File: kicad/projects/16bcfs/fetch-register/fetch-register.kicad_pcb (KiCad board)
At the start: 4 copper layers, 101.8 x 61 mm, 116 parts, among them J1 InstrReg, J10 Address Bus 2, J11 ALU Bus B, J12 Main Bus, J13 Control Signals, J14 Power, J15 Power, J2 MemBus1, J3 Address Bus 2, J4 ALU Bus B, J5 Main Bus, J6 Control Signals, J7 Power, J8 InstrReg, J9 MemBus1, U1 74HC541, U10 74HC541, U11 74HC574, U12 74HC574, U13 74HC541, U2 74HC541, U3 74HC541, U4 74HC541, U5 74HC541, U6 74HC541, U7 74HC541, U8 74HC541, U9 74HC541

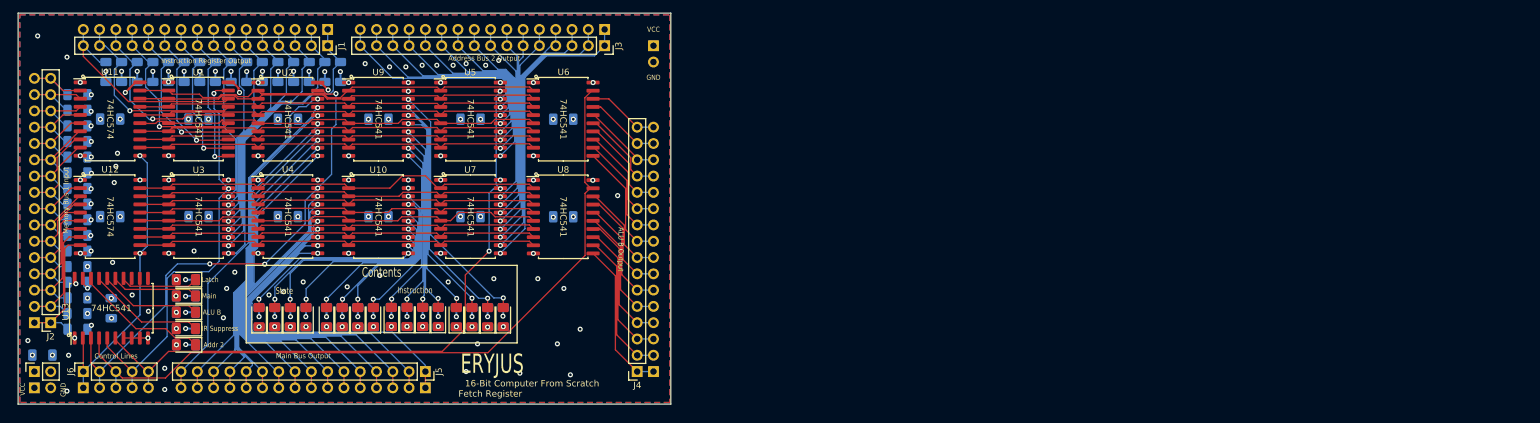
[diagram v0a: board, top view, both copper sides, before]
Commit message: Update the big-picture component placement
For the Fetch Register, all components needed to be removed and
re-placed into the PCB.  This commit is a first cut at that placement to
try to arrange the PCB.  The PCB can be shrunk quite a bit (maybe by
25%?) and this commit preceeds those changes.

Some changes were made to the schematic in order to drive more
efficient trace routing.
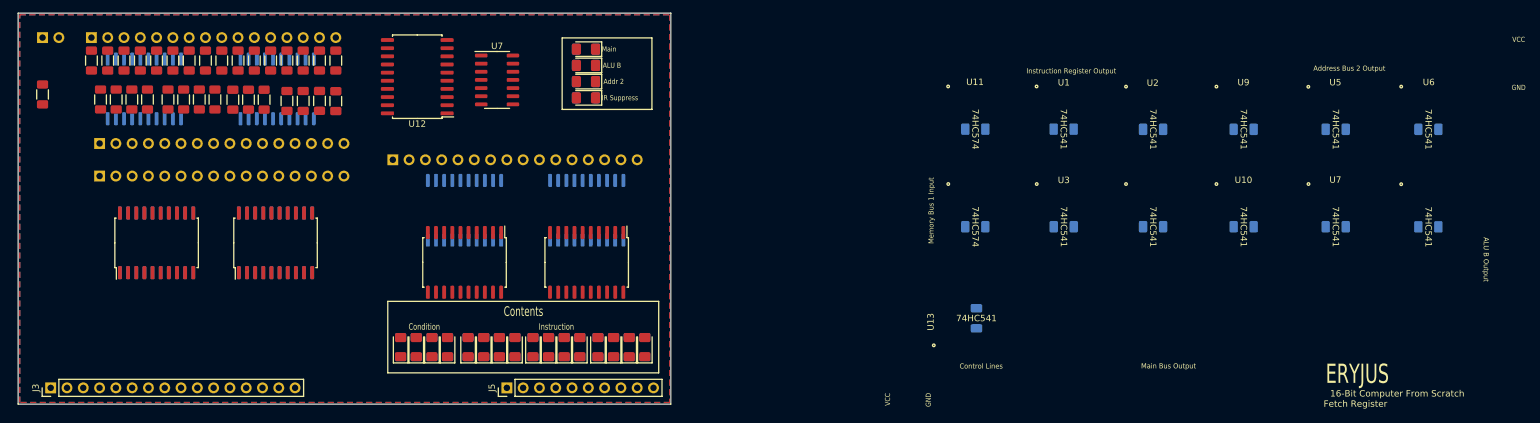
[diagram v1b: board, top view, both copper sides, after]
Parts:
- removed C14: 47uF, Capacitor_SMD:C_1206_3216Metric_Pad1.33x1.80mm_HandSolder
- removed D21: Red, LED_SMD:LED_1206_3216Metric_Pad1.42x1.75mm_HandSolder
- removed J10: Address Bus 2, Connector_PinHeader_2.54mm:PinHeader_1x16_P2.54mm_Vertical
- removed J11: ALU Bus B, Connector_PinHeader_2.54mm:PinHeader_1x16_P2.54mm_Vertical
- removed J12: Main Bus, Connector_PinHeader_2.54mm:PinHeader_1x16_P2.54mm_Vertical
- removed J13: Control Signals, Connector_PinHeader_2.54mm:PinHeader_1x05_P2.54mm_Vertical
- removed J14, J15: Power, Connector_PinHeader_2.54mm:PinHeader_1x02_P2.54mm_Vertical
- removed J8: InstrReg, Connector_PinHeader_2.54mm:PinHeader_1x16_P2.54mm_Vertical
- removed J9: MemBus1, Connector_PinHeader_2.54mm:PinHeader_1x16_P2.54mm_Vertical
- removed R53: 1K, Resistor_SMD:R_1206_3216Metric_Pad1.30x1.75mm_HandSolder
- removed U13: 74HC541, Package_SO:SOIC-20W_7.5x12.8mm_P1.27mm
- C12, C13: value 0.1uF -> 47uF
- J1: value InstrReg -> InstrRegInput; footprint Connector_PinSocket_2.54mm:PinSocket_1x16_P2.54mm_Vertical -> Connector_PinHeader_2.54mm:PinHeader_1x16_P2.54mm_Vertical; moved to B.Cu
- J2: value MemBus1 -> ALU Bus B; footprint Connector_PinSocket_2.54mm:PinSocket_1x16_P2.54mm_Vertical -> Connector_PinHeader_2.54mm:PinHeader_1x16_P2.54mm_Vertical; moved to B.Cu
- J3: value Address Bus 2 -> FetchBusInput; footprint Connector_PinSocket_2.54mm:PinSocket_1x16_P2.54mm_Vertical -> Connector_PinHeader_2.54mm:PinHeader_1x16_P2.54mm_Vertical
- J4: value ALU Bus B -> Main Bus; footprint Connector_PinSocket_2.54mm:PinSocket_1x16_P2.54mm_Vertical -> Connector_PinHeader_2.54mm:PinHeader_1x16_P2.54mm_Vertical; moved to B.Cu
- J5: value Main Bus -> Control Signals; footprint Connector_PinSocket_2.54mm:PinSocket_1x16_P2.54mm_Vertical -> Connector_PinHeader_2.54mm:PinHeader_1x10_P2.54mm_Vertical
- J6: value Control Signals -> Address Bus 2; footprint Connector_PinSocket_2.54mm:PinSocket_1x05_P2.54mm_Vertical -> Connector_PinHeader_2.54mm:PinHeader_1x16_P2.54mm_Vertical; moved to B.Cu
- J7: footprint Connector_PinSocket_2.54mm:PinSocket_1x02_P2.54mm_Vertical -> Connector_PinHeader_2.54mm:PinHeader_1x02_P2.54mm_Vertical; moved to B.Cu
- R21, R22, R23, R24, R25, R26, R27, R28, R29, R30, R31, R32, R33, R34, R35, R36, R37, R38, R39, R40, R41, R42, R43, R44, R45, R46, R47, R48, R49, R50, R51, R52: value 1K -> 10K; moved to F.Cu
- U1, U2, U5, U6: value 74HC541 -> 74HC574
- U10, U3, U4, U8, U9: value 74HC541 -> 74HC574; moved to B.Cu
- U11: moved to B.Cu
- U12: value 74HC574 -> 74HC541
- U7: value 74HC541 -> 74HC04; footprint Package_SO:SOIC-20W_7.5x12.8mm_P1.27mm -> Package_SO:SOIC-14_3.9x8.7mm_P1.27mm
- moved C10 134.9 mm to (213.9, 48.5)
- moved C2 134.9 mm to (199.8, 33.4)
- moved C4 134.9 mm to (199.8, 48.5)
- moved C5 134.9 mm to (228.3, 33.4)
- moved C7 134.9 mm to (228.3, 48.5)
- moved C9 134.9 mm to (213.9, 33.4)
- moved C1 134.9 mm to (185.9, 33.3)
- moved C13 134.9 mm to (172.3, 62.8)
- moved C3 134.9 mm to (185.9, 48.5)
- moved C6 134.9 mm to (242.7, 33.4)
- moved C8 134.9 mm to (242.7, 48.6)
- moved C11 134.9 mm to (172.1, 33.3)
- moved C12 134.9 mm to (172.1, 48.5)
- moved J3 101.5 mm to (27.9, 73.7), turned to 90 degrees
- moved R1 94.3 mm to (120.6, 67.3)
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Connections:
- D17 pad 1: /Latch LED -> /Main LED
- D18 pad 1: /Main LED -> /ALU B LED
- D19 pad 1: /ALU B LED -> /InstrReg LED
- D20 pad 1: /InstrReg LED -> /AddrBus2 LED
- J2 pad 1: MemBus1Bit0 -> ALUBBit0
- J2 pad 10: MemBus1Bit9 -> ALUBBit9
- J2 pad 11: MemBus1BitA -> ALUBBitA
- J2 pad 12: MemBus1BitB -> ALUBBitB
- J2 pad 13: MemBus1BitC -> ALUBBitC
- J2 pad 14: MemBus1BitD -> ALUBBitD
- J2 pad 15: MemBus1BitE -> ALUBBitE
- J2 pad 16: MemBus1BitF -> ALUBBitF
- J2 pad 2: MemBus1Bit1 -> ALUBBit1
- J2 pad 3: MemBus1Bit2 -> ALUBBit2
- J2 pad 4: MemBus1Bit3 -> ALUBBit3
- J2 pad 5: MemBus1Bit4 -> ALUBBit4
- J2 pad 6: MemBus1Bit5 -> ALUBBit5
- J2 pad 7: MemBus1Bit6 -> ALUBBit6
- J2 pad 8: MemBus1Bit7 -> ALUBBit7
- J2 pad 9: MemBus1Bit8 -> ALUBBit8
- J3 pad 1: AddrBus2Bit0 -> FetchBusBit0
- J3 pad 10: AddrBus2Bit9 -> FetchBusBit9
- J3 pad 11: AddrBus2BitA -> FetchBusBitA
- J3 pad 12: AddrBus2BitB -> FetchBusBitB
- J3 pad 13: AddrBus2BitC -> FetchBusBitC
- J3 pad 14: AddrBus2BitD -> FetchBusBitD
- J3 pad 15: AddrBus2BitE -> FetchBusBitE
- J3 pad 16: AddrBus2BitF -> FetchBusBitF
- J3 pad 2: AddrBus2Bit1 -> FetchBusBit1
- J3 pad 3: AddrBus2Bit2 -> FetchBusBit2
- J3 pad 4: AddrBus2Bit3 -> FetchBusBit3
- J3 pad 5: AddrBus2Bit4 -> FetchBusBit4
- J3 pad 6: AddrBus2Bit5 -> FetchBusBit5
- J3 pad 7: AddrBus2Bit6 -> FetchBusBit6
- J3 pad 8: AddrBus2Bit7 -> FetchBusBit7
- J3 pad 9: AddrBus2Bit8 -> FetchBusBit8
- J4 pad 1: ALUBBit0 -> MainBit0
- J4 pad 10: ALUBBit9 -> MainBit9
- J4 pad 11: ALUBBitA -> MainBitA
- J4 pad 12: ALUBBitB -> MainBitB
- J4 pad 13: ALUBBitC -> MainBitC
- J4 pad 14: ALUBBitD -> MainBitD
- J4 pad 15: ALUBBitE -> MainBitE
- J4 pad 16: ALUBBitF -> MainBitF
- J4 pad 2: ALUBBit1 -> MainBit1
- J4 pad 3: ALUBBit2 -> MainBit2
- J4 pad 4: ALUBBit3 -> MainBit3
- J4 pad 5: ALUBBit4 -> MainBit4
- J4 pad 6: ALUBBit5 -> MainBit5
- J4 pad 7: ALUBBit6 -> MainBit6
- J4 pad 8: ALUBBit7 -> MainBit7
- J4 pad 9: ALUBBit8 -> MainBit8
- J5 pad 1: MainBit0 -> CpuClk
- J5 pad 10: MainBit9 -> GNDREF
- J5 pad 2: MainBit1 -> GNDREF
- J5 pad 3: MainBit2 -> MainBusAssert
- J5 pad 4: MainBit3 -> ALUBAssert
- J5 pad 5: MainBit4 -> AddrBus2Assert
- J5 pad 6: MainBit5 -> InstrRegSuppress
- J5 pad 7: MainBit6 -> /Reset
- J5 pad 8: MainBit7 -> /~{RHLD}
- J5 pad 9: MainBit8 -> VCC
- J6 pad 1: RawCLK -> AddrBus2Bit0
- J6 pad 2: MainBusAssert -> AddrBus2Bit1
- J6 pad 3: ALUBAssert -> AddrBus2Bit2
- J6 pad 4: InstrRegSuppress -> AddrBus2Bit3
- J6 pad 5: AddrBus2Assert -> AddrBus2Bit4
- R1 pad 1: InstrRegBitF -> GNDREF
- R1 pad 2: GNDREF -> Net-(D1-K)
- R10 pad 1: InstrRegBit6 -> GNDREF
- R10 pad 2: GNDREF -> Net-(D10-K)
- R11 pad 1: InstrRegBit5 -> GNDREF
- R11 pad 2: GNDREF -> Net-(D11-K)
- R12 pad 1: InstrRegBit4 -> GNDREF
- R12 pad 2: GNDREF -> Net-(D12-K)
- R13 pad 1: InstrRegBit3 -> GNDREF
- R13 pad 2: GNDREF -> Net-(D13-K)
- R14 pad 1: InstrRegBit2 -> GNDREF
- R14 pad 2: GNDREF -> Net-(D14-K)
- R15 pad 1: InstrRegBit1 -> GNDREF
- R15 pad 2: GNDREF -> Net-(D15-K)
- R16 pad 1: InstrRegBit0 -> GNDREF
- R16 pad 2: GNDREF -> Net-(D16-K)
- R17 pad 1: MemBus1Bit0 -> VCC
- R17 pad 2: GNDREF -> Net-(D17-A)
- R18 pad 1: MemBus1Bit1 -> VCC
- R18 pad 2: GNDREF -> Net-(D18-A)
- R19 pad 1: MemBus1Bit2 -> VCC
- R19 pad 2: GNDREF -> Net-(D19-A)
- R2 pad 1: InstrRegBitE -> GNDREF
- R2 pad 2: GNDREF -> Net-(D2-K)
- R20 pad 1: MemBus1Bit3 -> VCC
- R20 pad 2: GNDREF -> Net-(D20-A)
- R21 pad 1: MemBus1Bit4 -> InstrRegBitF
- R22 pad 1: MemBus1Bit5 -> InstrRegBitE
- R23 pad 1: MemBus1Bit6 -> InstrRegBitD
- R24 pad 1: MemBus1Bit7 -> InstrRegBitC
- R25 pad 1: MemBus1Bit8 -> InstrRegBitB
- R26 pad 1: MemBus1Bit9 -> InstrRegBitA
- R27 pad 1: GNDREF -> InstrRegBit9
- R27 pad 2: Net-(D1-K) -> GNDREF
- R28 pad 1: MemBus1BitA -> InstrRegBit8
- R29 pad 1: GNDREF -> InstrRegBit7
- R29 pad 2: Net-(D2-K) -> GNDREF
- R3 pad 1: InstrRegBitD -> GNDREF
- R3 pad 2: GNDREF -> Net-(D3-K)
- R30 pad 1: MemBus1BitB -> InstrRegBit6
- R31 pad 1: GNDREF -> InstrRegBit5
- R31 pad 2: Net-(D3-K) -> GNDREF
- R32 pad 1: MemBus1BitC -> InstrRegBit4
- R33 pad 1: GNDREF -> InstrRegBit3
- R33 pad 2: Net-(D4-K) -> GNDREF
- R34 pad 1: MemBus1BitD -> InstrRegBit2
- R35 pad 1: GNDREF -> InstrRegBit1
- R35 pad 2: Net-(D5-K) -> GNDREF
- R36 pad 1: MemBus1BitE -> InstrRegBit0
- R37 pad 1: GNDREF -> FetchBusBit0
- R37 pad 2: Net-(D6-K) -> GNDREF
- R38 pad 1: MemBus1BitF -> FetchBusBit1
- R39 pad 1: GNDREF -> FetchBusBit2
- R39 pad 2: Net-(D7-K) -> GNDREF
- R4 pad 1: InstrRegBitC -> GNDREF
- R4 pad 2: GNDREF -> Net-(D4-K)
- R40 pad 1: GNDREF -> FetchBusBit3
- R40 pad 2: Net-(D8-K) -> GNDREF
- R41 pad 1: GNDREF -> FetchBusBit4
- R41 pad 2: Net-(D9-K) -> GNDREF
- R42 pad 1: GNDREF -> FetchBusBit5
- R42 pad 2: Net-(D10-K) -> GNDREF
- R43 pad 1: GNDREF -> FetchBusBit6
- R43 pad 2: Net-(D11-K) -> GNDREF
- R44 pad 1: GNDREF -> FetchBusBit7
- R44 pad 2: Net-(D12-K) -> GNDREF
- R45 pad 1: GNDREF -> FetchBusBit8
- R45 pad 2: Net-(D13-K) -> GNDREF
- R46 pad 1: GNDREF -> FetchBusBit9
- R46 pad 2: Net-(D14-K) -> GNDREF
- R47 pad 1: GNDREF -> FetchBusBitA
- R47 pad 2: Net-(D15-K) -> GNDREF
- R48 pad 1: GNDREF -> FetchBusBitB
- R48 pad 2: Net-(D16-K) -> GNDREF
- R49 pad 1: VCC -> FetchBusBitC
- R49 pad 2: Net-(D17-A) -> GNDREF
- R5 pad 1: InstrRegBitB -> GNDREF
- R5 pad 2: GNDREF -> Net-(D5-K)
- R50 pad 1: VCC -> FetchBusBitD
- R50 pad 2: Net-(D18-A) -> GNDREF
- R51 pad 1: VCC -> FetchBusBitE
- R51 pad 2: Net-(D19-A) -> GNDREF
- R52 pad 1: VCC -> FetchBusBitF
- R52 pad 2: Net-(D20-A) -> GNDREF
- R6 pad 1: InstrRegBitA -> GNDREF
- R6 pad 2: GNDREF -> Net-(D6-K)
- R7 pad 1: InstrRegBit9 -> GNDREF
- R7 pad 2: GNDREF -> Net-(D7-K)
- R8 pad 1: InstrRegBit8 -> GNDREF
- R8 pad 2: GNDREF -> Net-(D8-K)
- R9 pad 1: InstrRegBit7 -> GNDREF
- R9 pad 2: GNDREF -> Net-(D9-K)
- U1 pad 1: GNDREF -> ~{Addr 2 Assert}
- U1 pad 11: InstrRegBit8 -> CpuClk
- U1 pad 12: InstrRegBit9 -> AddrBus2Bit7
- U1 pad 13: InstrRegBitA -> AddrBus2Bit6
- U1 pad 14: InstrRegBitB -> AddrBus2Bit5
- U1 pad 15: InstrRegBitC -> AddrBus2Bit4
- U1 pad 16: InstrRegBitD -> AddrBus2Bit3
- U1 pad 17: InstrRegBitE -> AddrBus2Bit2
- U1 pad 18: InstrRegBitF -> AddrBus2Bit1
- U1 pad 19: InstrRegSuppress -> AddrBus2Bit0
- U1 pad 2: RegBitF -> FetchBusBit0
- U1 pad 3: RegBitE -> FetchBusBit1
- U1 pad 4: RegBitD -> FetchBusBit2
- U1 pad 5: RegBitC -> FetchBusBit3
- U1 pad 6: RegBitB -> FetchBusBit4
- U1 pad 7: RegBitA -> FetchBusBit5
- U1 pad 8: RegBit9 -> FetchBusBit6
- U1 pad 9: RegBit8 -> FetchBusBit7
- U10 pad 1: GNDREF -> ~{ALU B Assert}
- U10 pad 11: /Bit 0 LED -> CpuClk
- U10 pad 12: /Bit 1 LED -> ALUBBit8
- U10 pad 13: /Bit 2 LED -> ALUBBit9
- U10 pad 14: /Bit 3 LED -> ALUBBitA
- U10 pad 15: /Bit 4 LED -> ALUBBitB
- U10 pad 16: /Bit 5 LED -> ALUBBitC
- U10 pad 17: /Bit 6 LED -> ALUBBitD
- U10 pad 18: /Bit 7 LED -> ALUBBitE
- U10 pad 19: GNDREF -> ALUBBitF
- U10 pad 2: RegBit7 -> FetchBusBitF
- U10 pad 3: RegBit6 -> FetchBusBitE
- U10 pad 4: RegBit5 -> FetchBusBitD
- U10 pad 5: RegBit4 -> FetchBusBitC
- U10 pad 6: RegBit3 -> FetchBusBitB
- U10 pad 7: RegBit2 -> FetchBusBitA
- U10 pad 8: RegBit1 -> FetchBusBit9
- U10 pad 9: RegBit0 -> FetchBusBit8
- U11 pad 1: GNDREF -> ~{ALU B Assert}
- U11 pad 11: RawCLK -> CpuClk
- U11 pad 12: RegBit8 -> ALUBBit0
- U11 pad 13: RegBit9 -> ALUBBit1
- U11 pad 14: RegBitA -> ALUBBit2
- U11 pad 15: RegBitB -> ALUBBit3
- U11 pad 16: RegBitC -> ALUBBit4
- U11 pad 17: RegBitD -> ALUBBit5
- U11 pad 18: RegBitE -> ALUBBit6
- U11 pad 19: RegBitF -> ALUBBit7
- U11 pad 2: MemBus1BitF -> FetchBusBit7
- U11 pad 3: MemBus1BitE -> FetchBusBit6
- U11 pad 4: MemBus1BitD -> FetchBusBit5
- U11 pad 5: MemBus1BitC -> FetchBusBit4
- U11 pad 6: MemBus1BitB -> FetchBusBit3
- U11 pad 7: MemBus1BitA -> FetchBusBit2
- U11 pad 8: MemBus1Bit9 -> FetchBusBit1
- U11 pad 9: MemBus1Bit8 -> FetchBusBit0
- U12 pad 11: RawCLK -> unconnected-(U12-Y7-Pad11)
- U12 pad 12: RegBit0 -> unconnected-(U12-Y6-Pad12)
- U12 pad 13: RegBit1 -> unconnected-(U12-Y5-Pad13)
- U12 pad 14: RegBit2 -> unconnected-(U12-Y4-Pad14)
- U12 pad 15: RegBit3 -> /AddrBus2 LED
- U12 pad 16: RegBit4 -> /InstrReg LED
- U12 pad 17: RegBit5 -> /ALU B LED
- U12 pad 18: RegBit6 -> /Main LED
- U12 pad 19: RegBit7 -> GNDREF
- U12 pad 2: MemBus1Bit7 -> MainBusAssert
- U12 pad 3: MemBus1Bit6 -> ALUBAssert
- U12 pad 4: MemBus1Bit5 -> InstrRegSuppress
- U12 pad 5: MemBus1Bit4 -> AddrBus2Assert
- U12 pad 6: MemBus1Bit3 -> GNDREF
- U12 pad 7: MemBus1Bit2 -> GNDREF
- U12 pad 8: MemBus1Bit1 -> GNDREF
- U12 pad 9: MemBus1Bit0 -> GNDREF
- U2 pad 1: GNDREF -> ~{Addr 2 Assert}
- U2 pad 11: MainBit8 -> CpuClk
- U2 pad 12: MainBit9 -> AddrBus2BitF
- U2 pad 13: MainBitA -> AddrBus2BitE
- U2 pad 14: MainBitB -> AddrBus2BitD
- U2 pad 15: MainBitC -> AddrBus2BitC
- U2 pad 16: MainBitD -> AddrBus2BitB
- U2 pad 17: MainBitE -> AddrBus2BitA
- U2 pad 18: MainBitF -> AddrBus2Bit9
- U2 pad 19: MainBusAssert -> AddrBus2Bit8
- U2 pad 2: RegBitF -> FetchBusBit8
- U2 pad 3: RegBitE -> FetchBusBit9
- U2 pad 4: RegBitD -> FetchBusBitA
- U2 pad 5: RegBitC -> FetchBusBitB
- U2 pad 6: RegBitB -> FetchBusBitC
- U2 pad 7: RegBitA -> FetchBusBitD
- U2 pad 8: RegBit9 -> FetchBusBitE
- U2 pad 9: RegBit8 -> FetchBusBitF
- U3 pad 1: GNDREF -> InstrRegSuppress
- U3 pad 11: InstrRegBit0 -> CpuClk
- U3 pad 12: InstrRegBit1 -> InstrRegBit8
- U3 pad 13: InstrRegBit2 -> InstrRegBit9
- U3 pad 14: InstrRegBit3 -> InstrRegBitA
- U3 pad 15: InstrRegBit4 -> InstrRegBitB
- U3 pad 16: InstrRegBit5 -> InstrRegBitC
- U3 pad 17: InstrRegBit6 -> InstrRegBitD
- U3 pad 18: InstrRegBit7 -> InstrRegBitE
- U3 pad 19: InstrRegSuppress -> InstrRegBitF
- U3 pad 2: RegBit7 -> FetchBusBitF
- U3 pad 3: RegBit6 -> FetchBusBitE
- U3 pad 4: RegBit5 -> FetchBusBitD
- U3 pad 5: RegBit4 -> FetchBusBitC
- U3 pad 6: RegBit3 -> FetchBusBitB
- U3 pad 7: RegBit2 -> FetchBusBitA
- U3 pad 8: RegBit1 -> FetchBusBit9
- U3 pad 9: RegBit0 -> FetchBusBit8
- U4 pad 1: GNDREF -> InstrRegSuppress
- U4 pad 11: MainBit0 -> CpuClk
- U4 pad 12: MainBit1 -> InstrRegBit0
- U4 pad 13: MainBit2 -> InstrRegBit1
- U4 pad 14: MainBit3 -> InstrRegBit2
- U4 pad 15: MainBit4 -> InstrRegBit3
- U4 pad 16: MainBit5 -> InstrRegBit4
- U4 pad 17: MainBit6 -> InstrRegBit5
- U4 pad 18: MainBit7 -> InstrRegBit6
- U4 pad 19: MainBusAssert -> InstrRegBit7
- U4 pad 2: RegBit7 -> FetchBusBit7
- U4 pad 3: RegBit6 -> FetchBusBit6
- U4 pad 4: RegBit5 -> FetchBusBit5
- U4 pad 5: RegBit4 -> FetchBusBit4
- U4 pad 6: RegBit3 -> FetchBusBit3
- U4 pad 7: RegBit2 -> FetchBusBit2
- U4 pad 8: RegBit1 -> FetchBusBit1
- U4 pad 9: RegBit0 -> FetchBusBit0
- U5 pad 11: AddrBus2Bit8 -> CpuClk
- U5 pad 12: AddrBus2Bit9 -> /Bit 8 LED
- U5 pad 13: AddrBus2BitA -> /Bit 9 LED
- U5 pad 14: AddrBus2BitB -> /Bit A LED
- U5 pad 15: AddrBus2BitC -> /Bit B LED
- U5 pad 16: AddrBus2BitD -> /Bit C LED
- U5 pad 17: AddrBus2BitE -> /Bit D LED
- U5 pad 18: AddrBus2BitF -> /Bit E LED
- U5 pad 19: AddrBus2Assert -> /Bit F LED
- U5 pad 2: RegBitF -> FetchBusBitF
- U5 pad 3: RegBitE -> FetchBusBitE
- U5 pad 4: RegBitD -> FetchBusBitD
- U5 pad 5: RegBitC -> FetchBusBitC
- U5 pad 6: RegBitB -> FetchBusBitB
- U5 pad 7: RegBitA -> FetchBusBitA
- U5 pad 8: RegBit9 -> FetchBusBit9
- U5 pad 9: RegBit8 -> FetchBusBit8
- U6 pad 11: ALUBBit8 -> CpuClk
- U6 pad 12: ALUBBit9 -> /Bit 0 LED
- U6 pad 13: ALUBBitA -> /Bit 1 LED
- U6 pad 14: ALUBBitB -> /Bit 2 LED
- U6 pad 15: ALUBBitC -> /Bit 3 LED
- U6 pad 16: ALUBBitD -> /Bit 4 LED
- U6 pad 17: ALUBBitE -> /Bit 5 LED
- U6 pad 18: ALUBBitF -> /Bit 6 LED
- U6 pad 19: ALUBAssert -> /Bit 7 LED
- U6 pad 2: RegBitF -> FetchBusBit7
- U6 pad 3: RegBitE -> FetchBusBit6
- U6 pad 4: RegBitD -> FetchBusBit5
- U6 pad 5: RegBitC -> FetchBusBit4
- U6 pad 6: RegBitB -> FetchBusBit3
- U6 pad 7: RegBitA -> FetchBusBit2
- U6 pad 8: RegBit9 -> FetchBusBit1
- U6 pad 9: RegBit8 -> FetchBusBit0
- U7 pad 1: GNDREF -> MainBusAssert
- U7 pad 10: GNDREF -> unconnected-(U7-Pad10)
- U7 pad 11: AddrBus2Bit0 -> GNDREF
- U7 pad 12: AddrBus2Bit1 -> unconnected-(U7-Pad12)
- U7 pad 13: AddrBus2Bit2 -> GNDREF
- U7 pad 14: AddrBus2Bit3 -> VCC
- U7 pad 2: RegBit7 -> ~{Main Assert}
- U7 pad 3: RegBit6 -> ALUBAssert
- U7 pad 4: RegBit5 -> ~{ALU B Assert}
- U7 pad 5: RegBit4 -> AddrBus2Assert
- U7 pad 6: RegBit3 -> ~{Addr 2 Assert}
- U7 pad 7: RegBit2 -> GNDREF
- U7 pad 8: RegBit1 -> unconnected-(U7-Pad8)
- U7 pad 9: RegBit0 -> GNDREF
- U8 pad 1: GNDREF -> ~{Main Assert}
- U8 pad 11: ALUBBit0 -> CpuClk
- U8 pad 12: ALUBBit1 -> MainBit8
- U8 pad 13: ALUBBit2 -> MainBit9
- U8 pad 14: ALUBBit3 -> MainBitA
- U8 pad 15: ALUBBit4 -> MainBitB
- U8 pad 16: ALUBBit5 -> MainBitC
- U8 pad 17: ALUBBit6 -> MainBitD
- U8 pad 18: ALUBBit7 -> MainBitE
- U8 pad 19: ALUBAssert -> MainBitF
- U8 pad 2: RegBit7 -> FetchBusBitF
- U8 pad 3: RegBit6 -> FetchBusBitE
- U8 pad 4: RegBit5 -> FetchBusBitD
- U8 pad 5: RegBit4 -> FetchBusBitC
- U8 pad 6: RegBit3 -> FetchBusBitB
- U8 pad 7: RegBit2 -> FetchBusBitA
- U8 pad 8: RegBit1 -> FetchBusBit9
- U8 pad 9: RegBit0 -> FetchBusBit8
- U9 pad 1: GNDREF -> ~{Main Assert}
- U9 pad 11: /Bit 8 LED -> CpuClk
- U9 pad 12: /Bit 9 LED -> MainBit0
- U9 pad 13: /Bit A LED -> MainBit1
- U9 pad 14: /Bit B LED -> MainBit2
- U9 pad 15: /Bit C LED -> MainBit3
- U9 pad 16: /Bit D LED -> MainBit4
- U9 pad 17: /Bit E LED -> MainBit5
- U9 pad 18: /Bit F LED -> MainBit6
- U9 pad 19: GNDREF -> MainBit7
- U9 pad 2: RegBitF -> FetchBusBit7
- U9 pad 3: RegBitE -> FetchBusBit6
- U9 pad 4: RegBitD -> FetchBusBit5
- U9 pad 5: RegBitC -> FetchBusBit4
- U9 pad 6: RegBitB -> FetchBusBit3
- U9 pad 7: RegBitA -> FetchBusBit2
- U9 pad 8: RegBit9 -> FetchBusBit1
- U9 pad 9: RegBit8 -> FetchBusBit0
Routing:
- net GNDREF: track 494.7 -> 0.00 mm, vias 132 -> 0
- net VCC: track 337.7 -> 0.00 mm, vias 32 -> 0
- net ALUBAssert: track 118.2 -> 0.00 mm
- net AddrBus2Assert: track 102.5 -> 0.00 mm, vias 3 -> 0
- net MainBusAssert: track 78.1 -> 0.00 mm, vias 4 -> 0
- net InstrRegSuppress: track 65.7 -> 0.00 mm, vias 2 -> 0
- net RegBit7: track 64.5 -> 0.00 mm
- net RegBitF: track 64.4 -> 0.00 mm
- net RegBit3: track 64.0 -> 0.00 mm
- net RegBitB: track 63.6 -> 0.00 mm
- net RegBit5: track 63.4 -> 0.00 mm
- net RegBit4: track 63.4 -> 0.00 mm
- net RegBit1: track 63.4 -> 0.00 mm
- net RegBit6: track 63.4 -> 0.00 mm
- net RegBit0: track 63.3 -> 0.00 mm
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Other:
- board text added: "Condition"
- board text removed: "Latch"
- board text removed: "State"

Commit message: Collapse and Organize the left of the PCB
The left side of the PCB was organized with this commit.  It is reduced
in height by about 1/4 to 1/3.  This than sets the desired height for
the entire PCB.
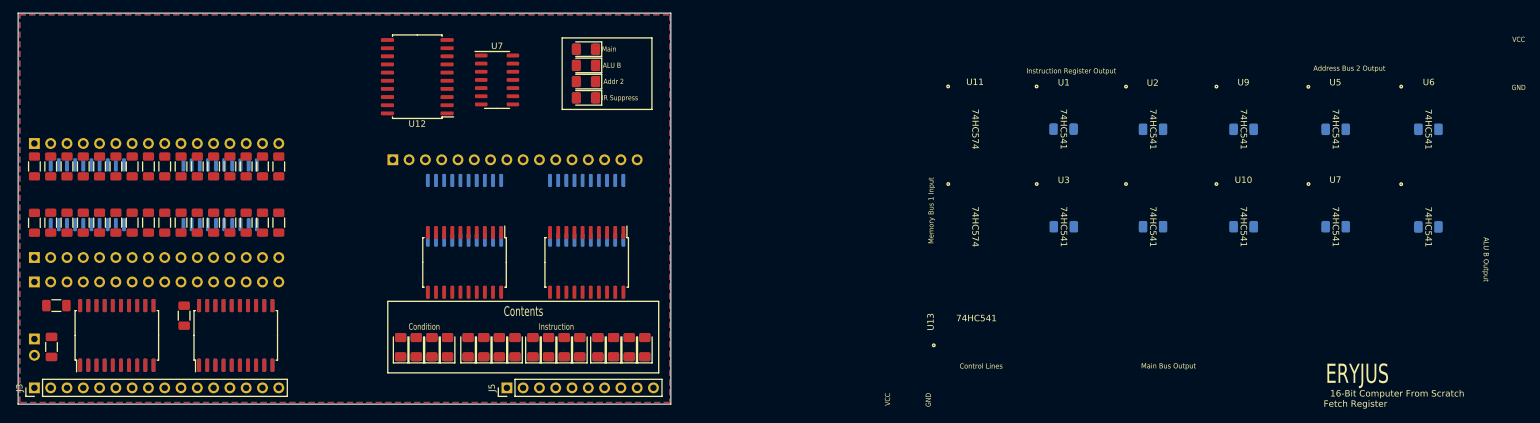
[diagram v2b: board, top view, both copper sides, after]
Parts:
- C11, C12, C13: moved to F.Cu
- moved C13 144.3 mm to (28.1, 67.3)
- moved C12 143.8 mm to (28.8, 60.8)
- moved C11 126.7 mm to (48.7, 62.4), turned to -90 degrees
- moved J7 47.0 mm to (25.4, 66.0), turned to 180 degrees
- moved R37 40.6 mm to (25.4, 47.9)
- moved R39 34.2 mm to (30.5, 47.9)
- moved R40 30.2 mm to (33.0, 47.9)
- moved R41 26.3 mm to (35.6, 47.9)
- moved R48 26.1 mm to (53.3, 47.9)
- moved R49 25.1 mm to (55.9, 47.9)
- moved R42 23.2 mm to (38.1, 47.9)
- moved R47 23.0 mm to (50.8, 47.9)
- moved R50 22.2 mm to (58.4, 47.9)
- moved R43 20.8 mm to (40.6, 47.9)
- moved R46 20.7 mm to (48.3, 47.9)
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
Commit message: Complete Component Placement on the Fetch Reg PCB
This commit handles all the component placement on the PCB for the Fetch
Register ahead of routing traces.  The expectation is that there is
plenty of room for traces.

Nothing has been done for 0R Resistors or test points yet.  Those will
be added ahead of routing.
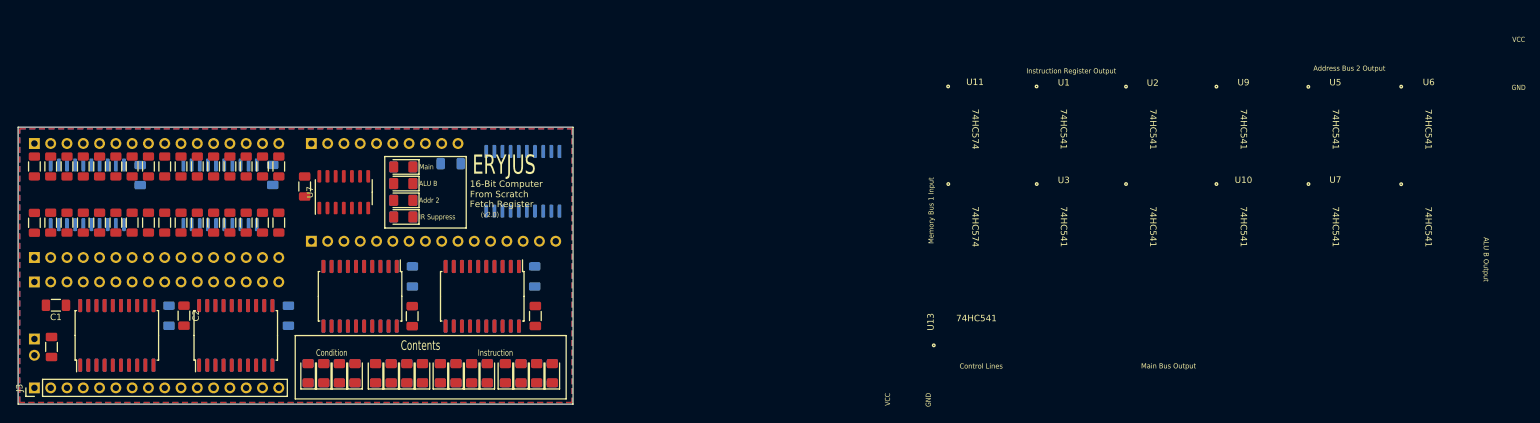
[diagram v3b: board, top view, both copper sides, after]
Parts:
- C1, C2, C5, C6, C7: moved to F.Cu
- C11, C12, J5, U12: moved to B.Cu
- moved C6 161.1 mm to (84.3, 62.5), turned to 90 degrees
- moved C7 160.9 mm to (67.5, 42.3), turned to -90 degrees
- moved C1 159.5 mm to (28.8, 60.8)
- moved C4 158.1 mm to (41.9, 40.5), turned to -90 degrees
- moved C2 153.9 mm to (48.7, 62.4), turned to -90 degrees
- moved C10 149.6 mm to (65.0, 62.4), turned to -90 degrees
- moved C8 139.5 mm to (103.4, 56.3), turned to -90 degrees
- moved C9 131.6 mm to (84.3, 56.3), turned to -90 degrees
- moved C5 128.1 mm to (103.5, 62.5), turned to 90 degrees
- moved C3 123.6 mm to (62.6, 40.5), turned to -90 degrees
- moved C12 65.3 mm to (90.3, 38.7), turned to 0 degrees
- moved J5 48.8 mm to (68.6, 35.6), turned to -90 degrees
- moved D20 38.7 mm to (82.9, 47.0)
- moved R20 38.7 mm to (82.9, 47.0)
- moved D19 35.4 mm to (82.9, 44.4)
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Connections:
- D19 pad 1: /InstrReg LED -> /AddrBus2 LED
- D20 pad 1: /AddrBus2 LED -> /InstrReg LED
- U12 pad 15: /AddrBus2 LED -> /InstrReg LED
- U12 pad 16: /InstrReg LED -> /AddrBus2 LED
- U12 pad 4: InstrRegSuppress -> AddrBus2Assert
- U12 pad 5: AddrBus2Assert -> InstrRegSuppress
- U7 pad 1: MainBusAssert -> GNDREF
- U7 pad 10: unconnected-(U7-Pad10) -> ~{ALU B Assert}
- U7 pad 11: GNDREF -> ALUBAssert
- U7 pad 12: unconnected-(U7-Pad12) -> ~{Main Assert}
- U7 pad 13: GNDREF -> MainBusAssert
- U7 pad 2: ~{Main Assert} -> unconnected-(U7-Pad2)
- U7 pad 3: ALUBAssert -> GNDREF
- U7 pad 4: ~{ALU B Assert} -> unconnected-(U7-Pad4)
- U7 pad 5: AddrBus2Assert -> GNDREF
- U7 pad 6: ~{Addr 2 Assert} -> unconnected-(U7-Pad6)
- U7 pad 8: unconnected-(U7-Pad8) -> ~{Addr 2 Assert}
- U7 pad 9: GNDREF -> AddrBus2Assert
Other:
- board size 101.8 x 61 mm -> 86.5 x 43.2 mm
- board text added: "(v2.0)"

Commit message: Add 0R Resistors and Test Points to the PCB
Get this done before routing the PCB
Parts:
- added R53: 0R, Resistor_SMD:R_1206_3216Metric_Pad1.30x1.75mm_HandSolder, F.Cu at (100.5, 35.8)
- added R54: 0R, Resistor_SMD:R_1206_3216Metric_Pad1.30x1.75mm_HandSolder, F.Cu at (103.0, 35.8)
- added R55: 0R, Resistor_SMD:R_1206_3216Metric_Pad1.30x1.75mm_HandSolder, F.Cu at (105.5, 35.8)
- added R56: 0R, Resistor_SMD:R_1206_3216Metric_Pad1.30x1.75mm_HandSolder, F.Cu at (107.9, 35.8)
- added R57: 0R, Resistor_SMD:R_1206_3216Metric_Pad1.30x1.75mm_HandSolder, B.Cu at (71.2, 43.2)
- added R58: 0R, Resistor_SMD:R_1206_3216Metric_Pad1.30x1.75mm_HandSolder, B.Cu at (73.6, 43.2)
- added R59: 0R, Resistor_SMD:R_1206_3216Metric_Pad1.30x1.75mm_HandSolder, B.Cu at (76.2, 43.2)
- added TP1: TestPoint, eryjus:TestPoint_SMD_D0.8mm, F.Cu at (103.5, 48.8)
- added TP2: TestPoint, eryjus:TestPoint_SMD_D0.8mm, F.Cu at (104.7, 48.8)
- added TP3: TestPoint, eryjus:TestPoint_SMD_D0.8mm, F.Cu at (106.0, 48.8)
- added TP4: TestPoint, eryjus:TestPoint_SMD_D0.8mm, F.Cu at (107.3, 48.8)
- added TP5: TestPoint, eryjus:TestPoint_SMD_D0.8mm, F.Cu at (76.2, 48.8)
- added TP6: TestPoint, eryjus:TestPoint_SMD_D0.8mm, F.Cu at (73.6, 48.8)
- added TP7: TestPoint, eryjus:TestPoint_SMD_D0.8mm, F.Cu at (71.1, 48.8)
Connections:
- U12 pad 11: unconnected-(U12-Y7-Pad11) -> Net-(U12-Y7)
- U12 pad 12: unconnected-(U12-Y6-Pad12) -> Net-(U12-Y6)
- U12 pad 13: unconnected-(U12-Y5-Pad13) -> Net-(U12-Y5)
- U12 pad 14: unconnected-(U12-Y4-Pad14) -> Net-(U12-Y4)
- U12 pad 6: GNDREF -> Net-(U12-A4)
- U12 pad 7: GNDREF -> Net-(U12-A5)
- U12 pad 8: GNDREF -> Net-(U12-A6)
- U12 pad 9: GNDREF -> Net-(U12-A7)
- U7 pad 1: GNDREF -> Net-(R57-Pad2)
- U7 pad 2: unconnected-(U7-Pad2) -> Net-(TP7-Pad1)
- U7 pad 3: GNDREF -> Net-(R58-Pad2)
- U7 pad 4: unconnected-(U7-Pad4) -> Net-(TP6-Pad1)
- U7 pad 5: GNDREF -> Net-(R59-Pad2)
- U7 pad 6: unconnected-(U7-Pad6) -> Net-(TP5-Pad1)

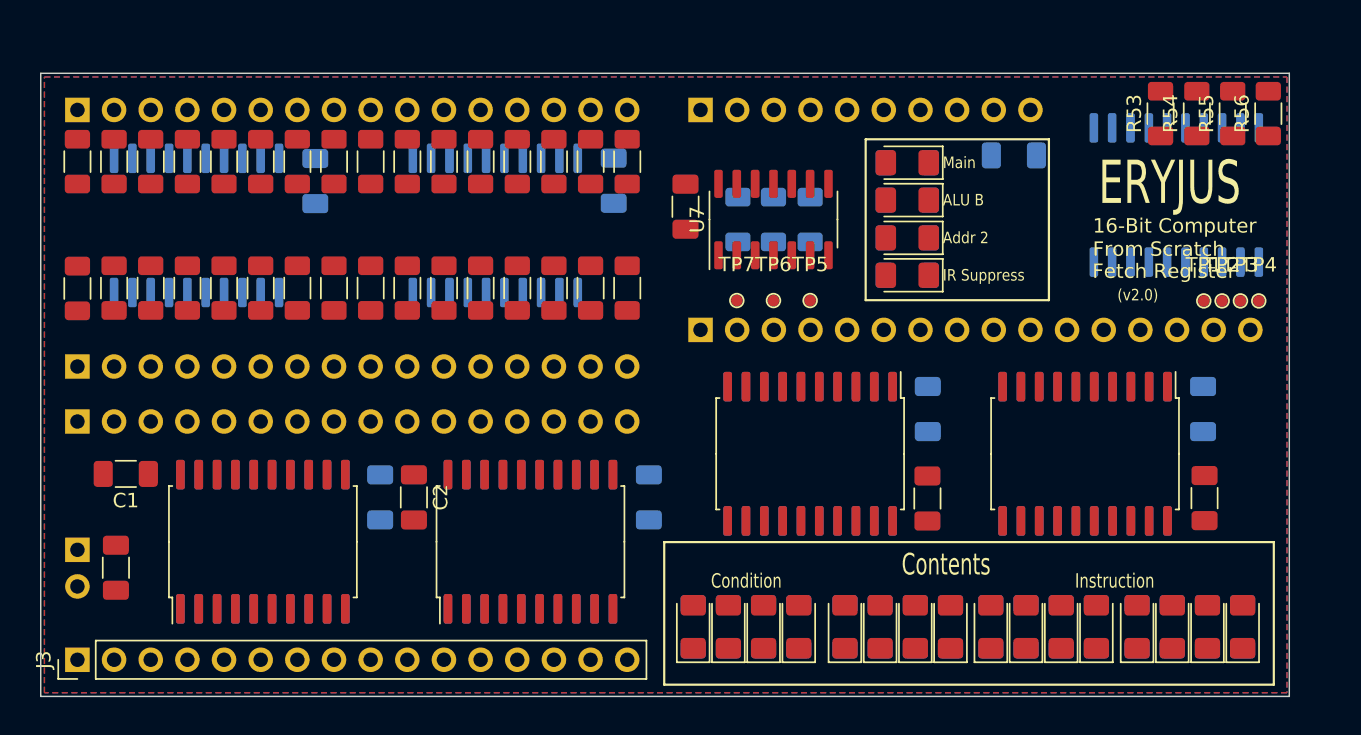
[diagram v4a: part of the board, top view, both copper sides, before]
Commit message: Complete the routing for the Fetch Register PCB
This commit completes the routing for the PCB, unless something needs to
move to make room for silkscreen.
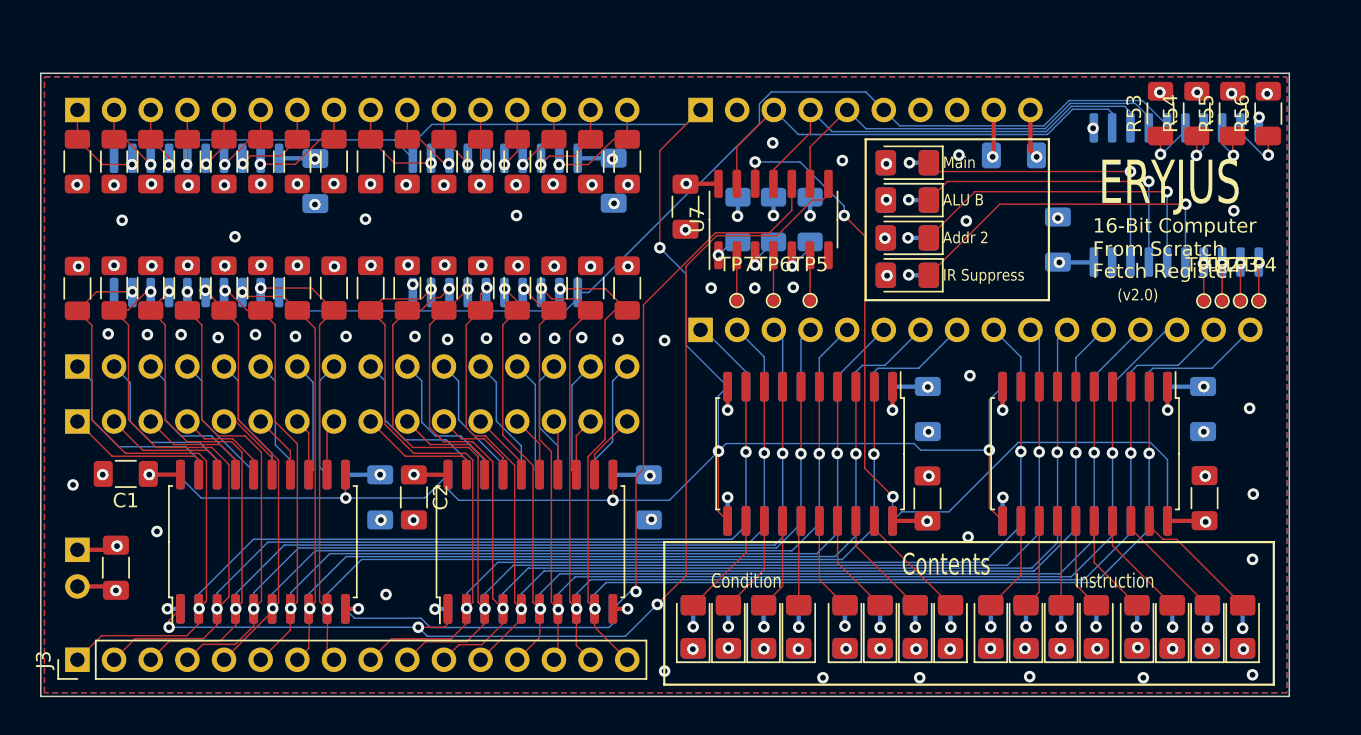
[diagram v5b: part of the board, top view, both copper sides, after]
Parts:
- added C14: 0.1uF, Capacitor_SMD:C_1206_3216Metric_Pad1.33x1.80mm_HandSolder, B.Cu at (93.3, 44.5)
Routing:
- net CpuClk: track 0.00 -> 150.6 mm, vias 0 -> 5
- net FetchBusBit0: track 0.00 -> 93.0 mm, vias 0 -> 3
- net FetchBusBit8: track 0.00 -> 90.5 mm, vias 0 -> 3
- net FetchBusBit1: track 0.00 -> 89.6 mm, vias 0 -> 3
- net FetchBusBit9: track 0.00 -> 88.3 mm, vias 0 -> 3
- net FetchBusBit2: track 0.00 -> 86.2 mm, vias 0 -> 3
- net FetchBusBitA: track 0.00 -> 84.6 mm, vias 0 -> 3
- net FetchBusBitF: track 0.00 -> 83.4 mm, vias 0 -> 3
- net FetchBusBit3: track 0.00 -> 82.7 mm, vias 0 -> 3
- net FetchBusBit7: track 0.00 -> 81.4 mm, vias 0 -> 3
- net FetchBusBitE: track 0.00 -> 80.8 mm, vias 0 -> 3
- net FetchBusBitB: track 0.00 -> 80.8 mm, vias 0 -> 3
- net FetchBusBit6: track 0.00 -> 80.6 mm, vias 0 -> 3
- net FetchBusBit5: track 0.00 -> 80.3 mm, vias 0 -> 3
- net FetchBusBitC: track 0.00 -> 79.8 mm, vias 0 -> 3
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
